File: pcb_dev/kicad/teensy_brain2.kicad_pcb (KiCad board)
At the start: 2 copper layers, 139.8 x 100.2 mm, 93 parts, among them IC1 INA118PB, IC2 INA118PB, IC3 INA118PB, IC4 INA118PB, J1 teensy4.1, P1 0026013115, P2 0026013115, P3 0026013115, P4 0026013115, U1 REF2033QDDCRQ1

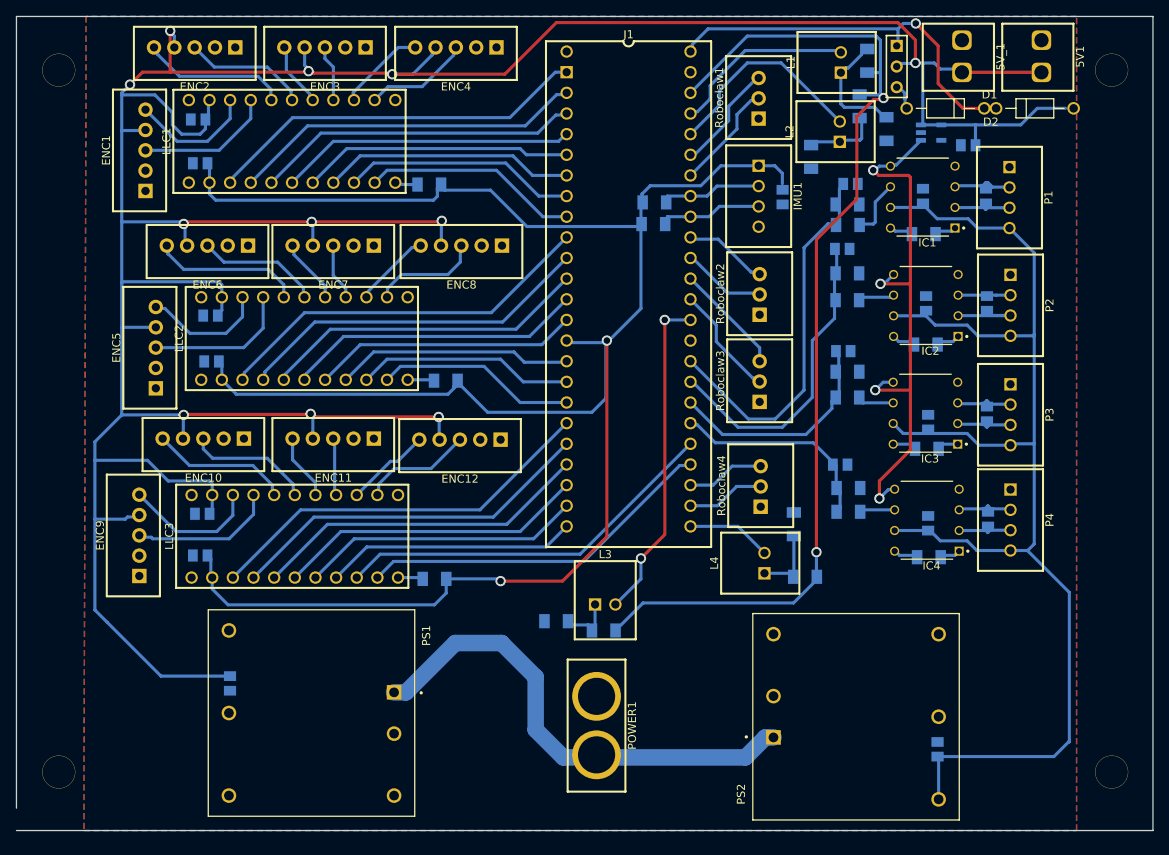
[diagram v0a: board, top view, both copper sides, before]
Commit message: fixed capacitor orientation
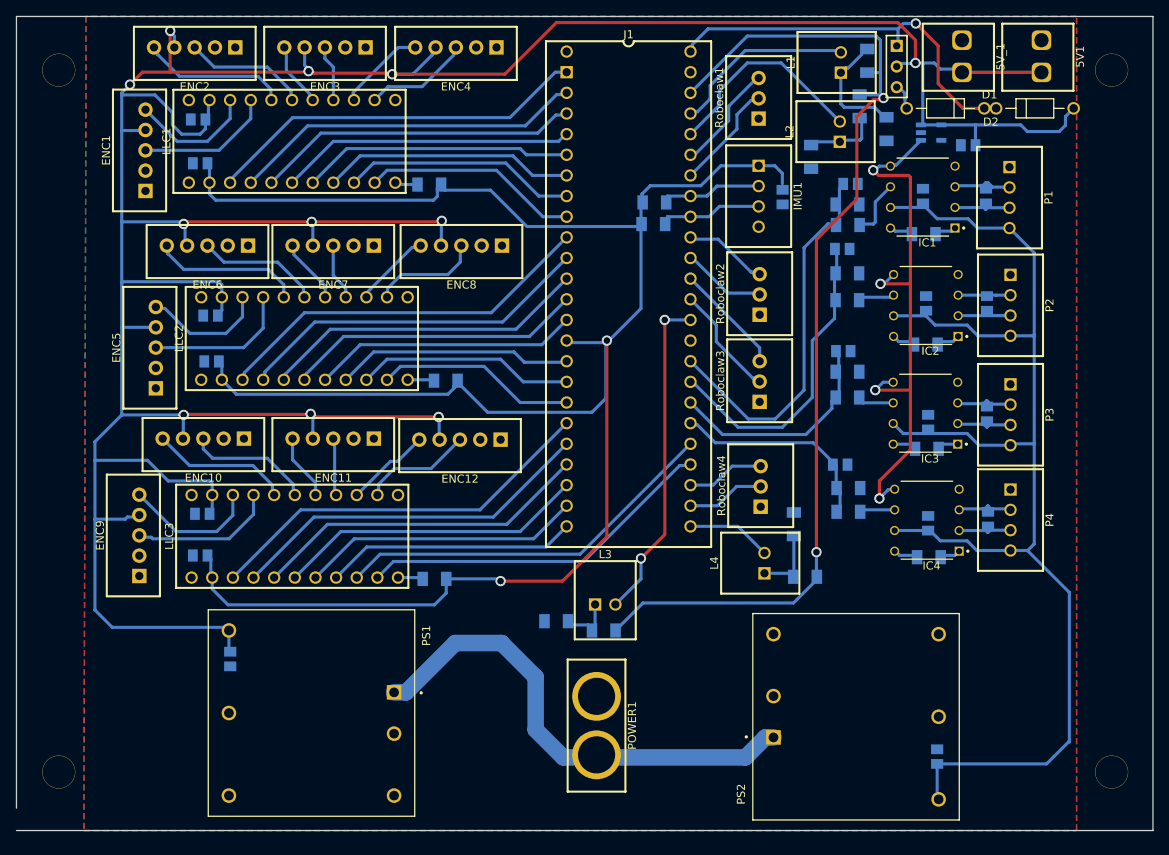
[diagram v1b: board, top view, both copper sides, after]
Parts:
- moved C19 3.00 mm to (104.9, 135.4), turned to -90 degrees
- moved C20 0.90 mm to (191.9, 147.4), turned to 90 degrees
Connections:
- C19 pad 1: GND -> 5V
- C19 pad 2: 5V -> GND
- C20 pad 1: GND -> 12V
- C20 pad 2: 12V -> GND
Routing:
- net 5V: track 427.5 -> 430.0 mm
- net 12V: track 160.0 -> 159.0 mm

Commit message: adjusted border spacings
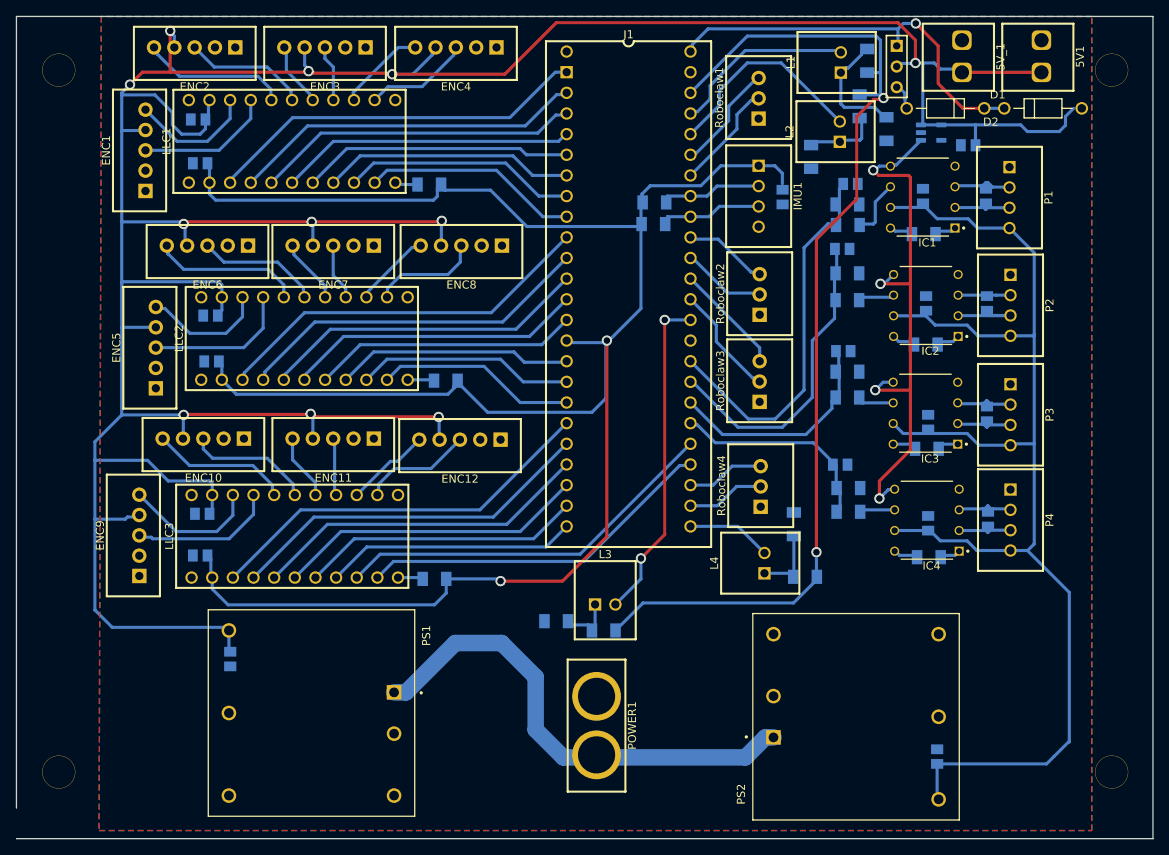
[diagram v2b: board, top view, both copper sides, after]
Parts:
- moved D1 1.00 mm to (204.9, 67.6)
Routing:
- net Vin: track 49.0 -> 50.0 mm
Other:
- board size 139.8 x 100.2 mm -> 139.8 x 101.2 mm
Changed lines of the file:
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@@
 	(footprint "diode:On_Semiconductor-1N4001G-Manufacturer_Recommended"
 		(layer "F.Cu")
-		(at 203.8874 67.6021)
+		(at 204.8874 67.6021)
 		(property "Reference" "D1"
 			(at -6.545 -1.674999 0)
@@
 	)
 	(gr_line
-		(start 78.5876 156.45931)
-		(end 218.41459 156.45931)
+		(start 78.5876 157.45931)
+		(end 218.41459 157.45931)
 		(stroke
 			(width 0.05)
@@
 	)
 	(gr_line
-		(start 218.41459 156.45931)
+		(start 218.41459 157.45931)
 		(end 218.4146 56.2991)
 		(stroke
@@
 	)
 	(gr_line
-		(start 218.41459 156.45931)
+		(start 218.41459 157.45931)
 		(end 218.4146 56.2991)
 		(stroke
@@
 	)
 	(gr_line
-		(start 78.5876 156.45931)
-		(end 218.41459 156.45931)
+		(start 78.5876 157.45931)
+		(end 218.41459 157.45931)
 		(stroke
 			(width 0.254)
@@
 	)
 	(gr_line
-		(start 78.5876 156.45931)
+		(start 78.5876 157.45931)
 		(end 78.5876 56.2991)
 		(stroke
@@
 	)
 	(segment
-		(start 197.6524 67.6021)
-		(end 199.1224 67.6021)
+		(start 197.657401 67.6021)
+		(end 200.117399 67.6021)
 		(width 0.381)
 		(layer "B.Cu")
@@
 		(polygon
 			(pts
-				(xy 86.8874 156.45931) (xy 209.0166 156.45931) (xy 209.0166 56.2991) (xy 87.15992 56.2991)
+				(xy 88.7582 156.45931) (xy 210.8874 156.45931) (xy 210.8874 56.2991) (xy 89.03072 56.2991)
 			)
 		)
@@
 		(polygon
 			(pts
-				(xy 86.8874 156.45931) (xy 209.0166 156.45931) (xy 209.0166 56.2991) (xy 87.16009 56.2991)
+				(xy 88.7582 156.45931) (xy 210.8874 156.45931) (xy 210.8874 56.2991) (xy 89.03089 56.2991)
 			)
 		)

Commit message: added correct 3D file model for ic chip and fixed visual appearance
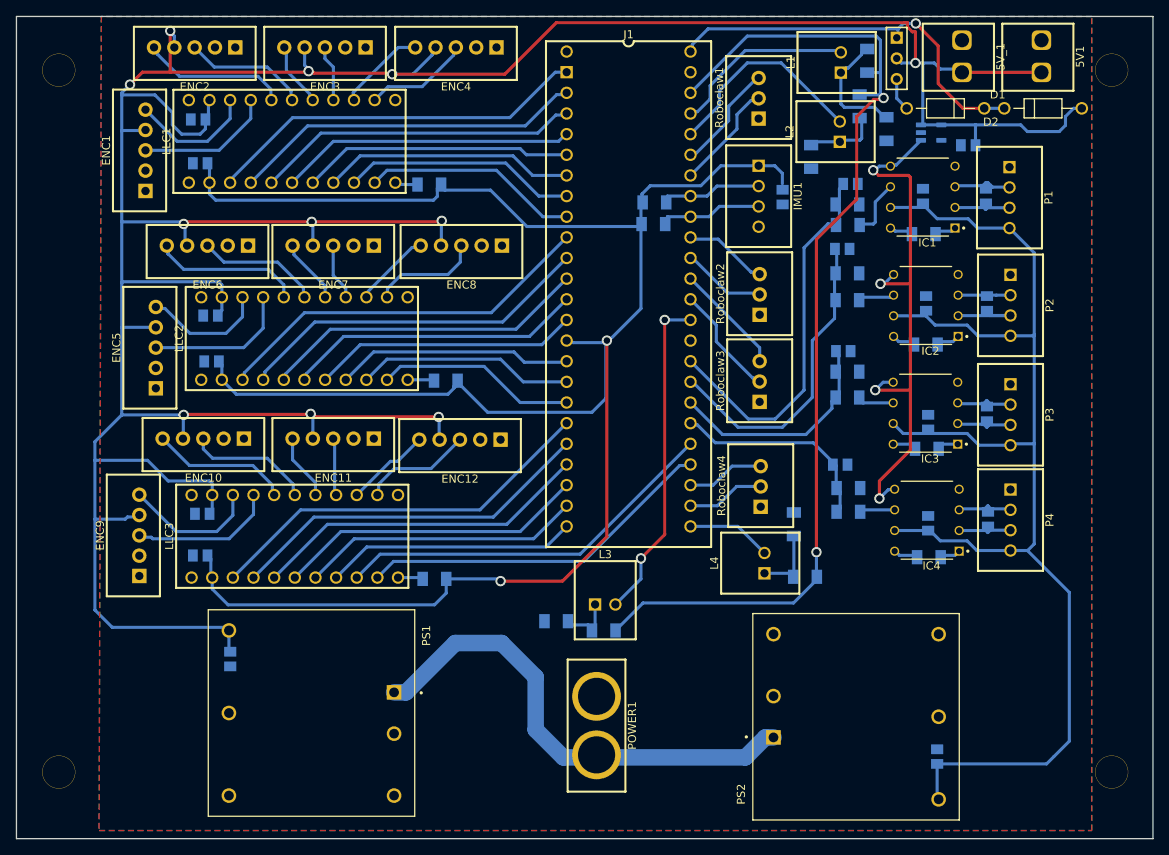
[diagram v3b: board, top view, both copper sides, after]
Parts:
- moved VUSB1 1.00 mm to (184.9, 50.0)
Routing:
- net 5V: track 430.0 -> 431.7 mm
- net Vin: track 50.0 -> 48.6 mm
- net VUSB: track 3.57 -> 4.15 mm
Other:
- outline, holes or cut-outs redrawn
